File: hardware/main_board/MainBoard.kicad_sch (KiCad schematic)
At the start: 68 parts, among them J1 5V In, J11 Conn_01x01, J12 GREEN, J13 Conn_01x05, J14 Conn_01x04, J2 9V In, J3 Conn_01x08, J4 Conn_01x08, J5 Conn_01x08, J6 Conn_01x08, J7 Conn_01x02, J8 Conn_01x10, J9 Conn_01x02, U1 TPIC6595, U2 ESP32-C6, U3 SD_Breakout, U4 TPIC6595, U5 TPIC6595, U6 TPIC6595, U7 74HC165

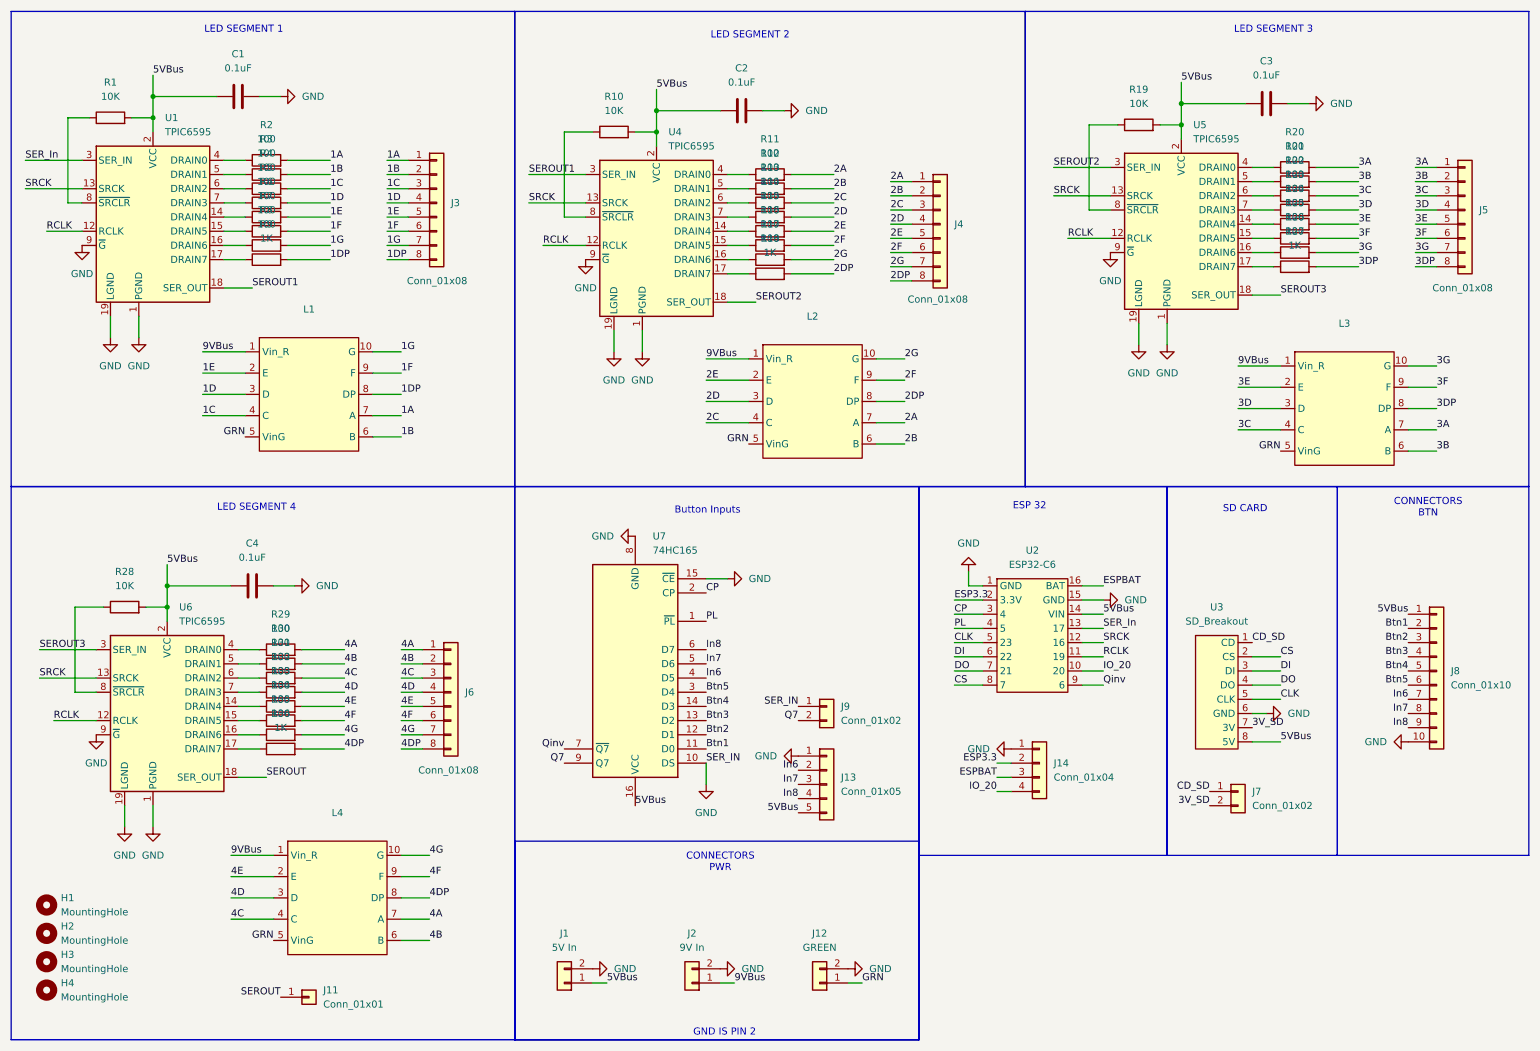
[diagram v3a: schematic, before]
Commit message: Started 2 layer mainboard, switching to 4 layer
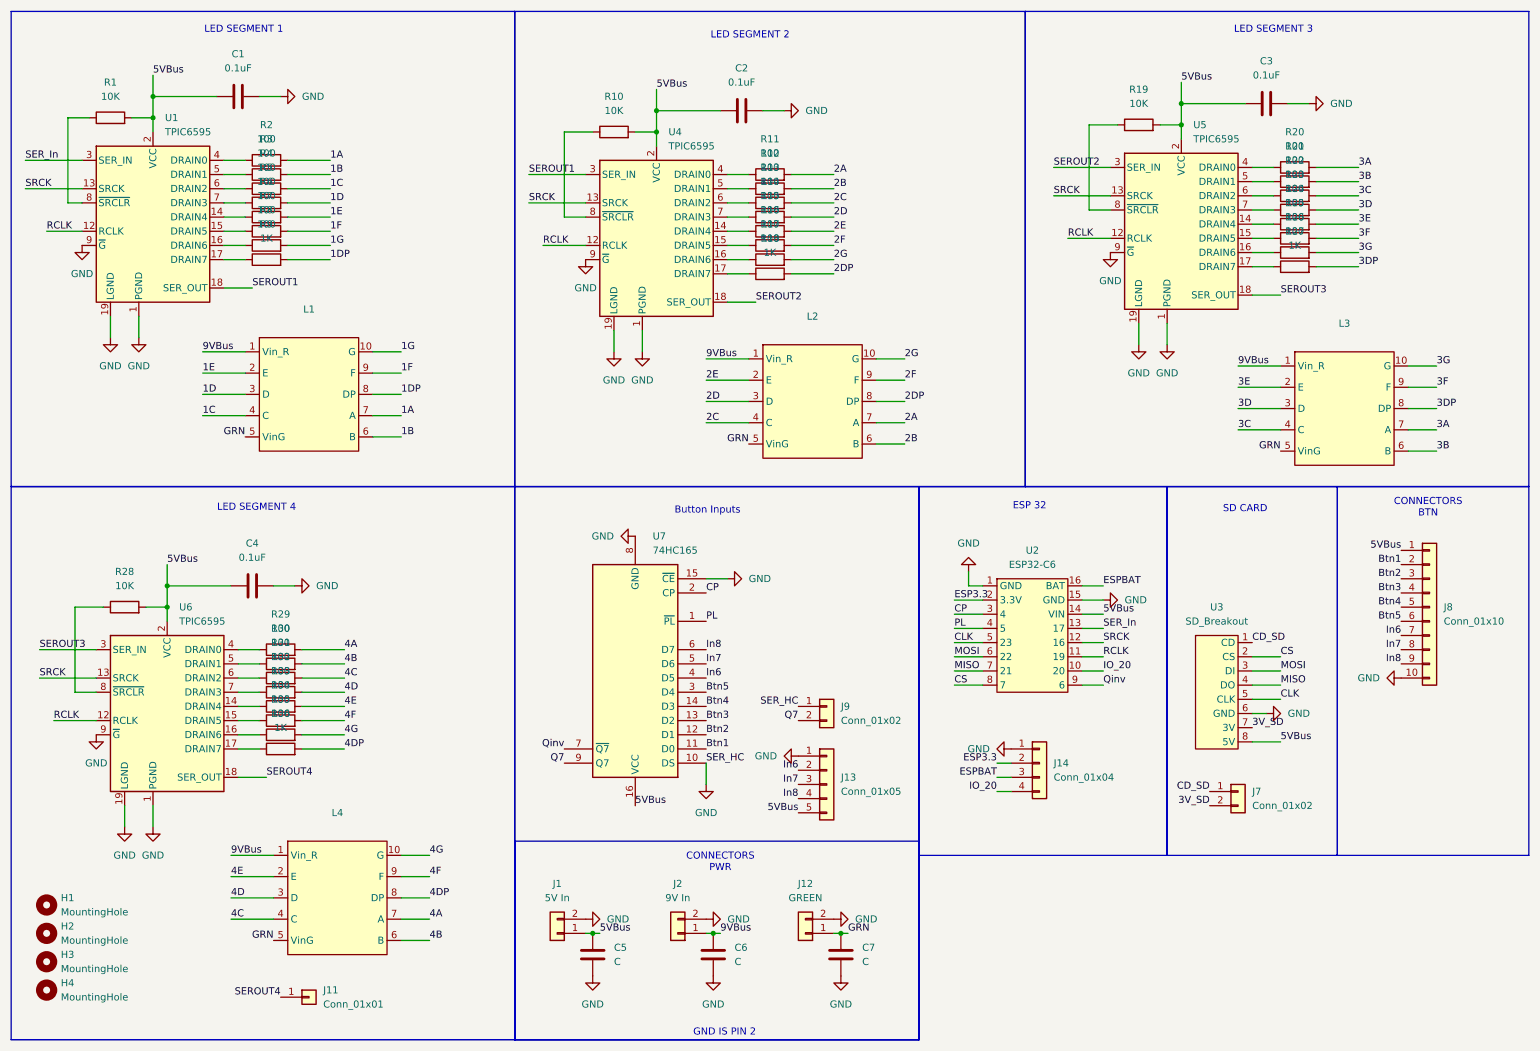
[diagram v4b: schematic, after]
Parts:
- removed J3, J4, J5, J6: Conn_01x08, Connector_PinHeader_2.54mm:PinHeader_1x08_P2.54mm_Vertical, symbol Connector_Generic:Conn_01x08
- added C5, C6, C7: C, Capacitor_SMD:C_1206_3216Metric_Pad1.33x1.80mm_HandSolder, symbol Device:C
- U3: footprint Connector_PinHeader_2.54mm:PinHeader_1x08_P2.54mm_Vertical -> GregFootprints:SD Card
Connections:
- net 5VBus: now also C5.1
- net 9VBus: now also C6.1
- net GND: now also C5.2, C6.2, C7.2
- net GRN: now also C7.1
- net DI renamed MOSI
- net DO renamed MISO
- net SEROUT renamed SEROUT4
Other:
- moved on the sheet: J1, J12, J2, J8
